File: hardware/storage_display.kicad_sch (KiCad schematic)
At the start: 0 parts

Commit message: Complete schematic, place and partially route the PCB
Schematic:
- Add Storage & Display sheet (microSD, FH12 OLED connector, TLV75801
  3.8 V VBAT regulator, charge-pump parts) and Radio sheet fixes
- Select remaining parts (PTS810, 1206L075THYR, SMF5.0A, MCP120 EN
  supervisor DNP, Elna DSK backup cap), add mounting holes and fiducials
- Pin changes for routability: PPS -> IO15, LoRa MOSI -> IO47,
  LoRa RESET -> IO48, LoRa DIO0 -> IO1
- Remove optional SPI clock filter parts (R309/C307, R310/C308)
- Remove company name from title blocks (personal project)

PCB (60 x 120 mm, 4 layers):
- Place all parts; GNSS zone with custom DRC rules (kicad_dru)
- Project ESP32-S3-WROOM-1 footprint with 0.4 mm thermal vias
- GND / +3V3 / +5V copper zones
- Route power path, GNSS, microSD and LoRa buses
- DRC clean except unrouted nets and expected silkscreen-at-edge items

Docs: selected-parts table, pin table and EMC deviation in PCB_DESIGN.md

Co-Authored-By: Claude Opus 5.5 <noreply@anthropic.com>
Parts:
- added C501: 100uF, Capacitor_SMD:C_1210_3225Metric, symbol Device:C
- added C502: 10uF, Capacitor_SMD:C_0805_2012Metric, symbol Device:C
- added C503: 100nF, Capacitor_SMD:C_0402_1005Metric, symbol Device:C
- added C504, C505, C506, C507, C510, C511: 1uF, Capacitor_SMD:C_0402_1005Metric, symbol Device:C
- added C508: 2.2uF, Capacitor_SMD:C_0603_1608Metric, symbol Device:C
- added C509: 4.7uF, Capacitor_SMD:C_0603_1608Metric, symbol Device:C
- added J501: DM3AT-SF-PEJM5, Connector_Card:microSD_HC_Hirose_DM3AT-SF-PEJM5, symbol Connector:Micro_SD_Card_Det2
- added J502: FH12-30S-0.5SH(55), Connector_FFC-FPC:Hirose_FH12-30S-0.5SH_1x30-1MP_P0.50mm_Horizontal, symbol Connector_Generic_MountingPin:Conn_01x30_MountingPin
- added R501, R502, R503, R504: 47k, Resistor_SMD:R_0402_1005Metric, symbol Device:R
- added R505, R510: 10k, Resistor_SMD:R_0402_1005Metric, symbol Device:R
- added R506, R507: 4.7k, Resistor_SMD:R_0402_1005Metric, symbol Device:R
- added R508: 390k, Resistor_SMD:R_0402_1005Metric, symbol Device:R
- added R509: 59k, Resistor_SMD:R_0402_1005Metric, symbol Device:R
- added TP501: VBAT, TestPoint:TestPoint_Pad_D1.0mm, symbol Connector:TestPoint
- added U501: TLV75801PDBV, Package_TO_SOT_SMD:SOT-23-5, symbol Regulator_Linear:TLV75801PDBV
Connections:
- new net: R509.2, R510.1, U501.4 (FB)
- new net +3V3: C501.1, C502.1, C503.1, C507.1, J501.4 (VDD), J502.11 (Pin_11), J502.9 (Pin_9), R501.1, R502.1, R503.1, R504.1, R505.1, R506.1, R507.1
- new net +5V: C510.1, U501.1 (IN), U501.3 (EN)
- new net GND: C501.2, C502.2, C503.2, C506.2, C507.2, C508.2, C509.2, C510.2, C511.2, J501.6 (VSS), J501.SH (SHIELD), J502.1 (Pin_1), J502.10 (Pin_10), J502.12 (Pin_12), J502.13 (Pin_13), J502.15 (Pin_15), J502.16 (Pin_16), J502.17 (Pin_17), J502.21 (Pin_21), J502.22 (Pin_22), J502.23 (Pin_23), J502.24 (Pin_24), J502.25 (Pin_25), J502.29 (Pin_29), J502.30 (Pin_30), J502.8 (Pin_8), J502.MP (MountPin), R508.2, R510.2, U501.2 (GND)
- new net OLED_C1N: C505.2, J502.5 (Pin_5)
- new net OLED_C1P: C505.1, J502.4 (Pin_4)
- new net OLED_C2N: C504.2, J502.2 (Pin_2)
- new net OLED_C2P: C504.1, J502.3 (Pin_3)
- new net OLED_IREF: J502.26 (Pin_26), R508.1
- new net OLED_RES: J502.14 (Pin_14), R505.2
- new net OLED_SCL: J502.18 (Pin_18), R507.2
- new net OLED_SDA: J502.19 (Pin_19), J502.20 (Pin_20), R506.2
- new net OLED_VBAT: C506.1, C511.1, J502.6 (Pin_6), R509.1, TP501.1, U501.5 (OUT)
- new net OLED_VCC: C508.1, J502.28 (Pin_28)
- new net OLED_VCOMH: C509.1, J502.27 (Pin_27)
- new net SD_CS: J501.2 (DAT3/CD), R502.2
- new net SD_DAT1: J501.8 (DAT1), R504.2
- new net SD_DAT2: J501.1 (DAT2), R501.2
- new net SD_MISO: J501.7 (DAT0), R503.2
- new net SD_MOSI: J501.3 (CMD)
- new net SD_SCK: J501.5 (CLK)
- no-connect marks 0 -> 3
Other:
- note added: "47k pull-ups on CS, DAT0, DAT1, DAT2. Card detect unused in v1."
- note added: "C504/C505 charge pump, C508 VCC, C509 VCOMH, R508 IREF"
- note added: "OLED: EastRising ER-OLED0.96-1.1W on Hirose FH12 (bottom contact). Values from panel datasheet sec. 1.6.2."
- note added: "Pin = panel FPC pin"
- note added: "VBAT 3.8 V: Vout = 0.55 V x (1 + 59k/10k) = 3.795 V (panel window 3.5-4.2 V). VCC/VCOMH caps rated 16 V or more."
- note added: "microSD (SPI mode, 3.3 V)"
- company: SSS-Defence -> (none)

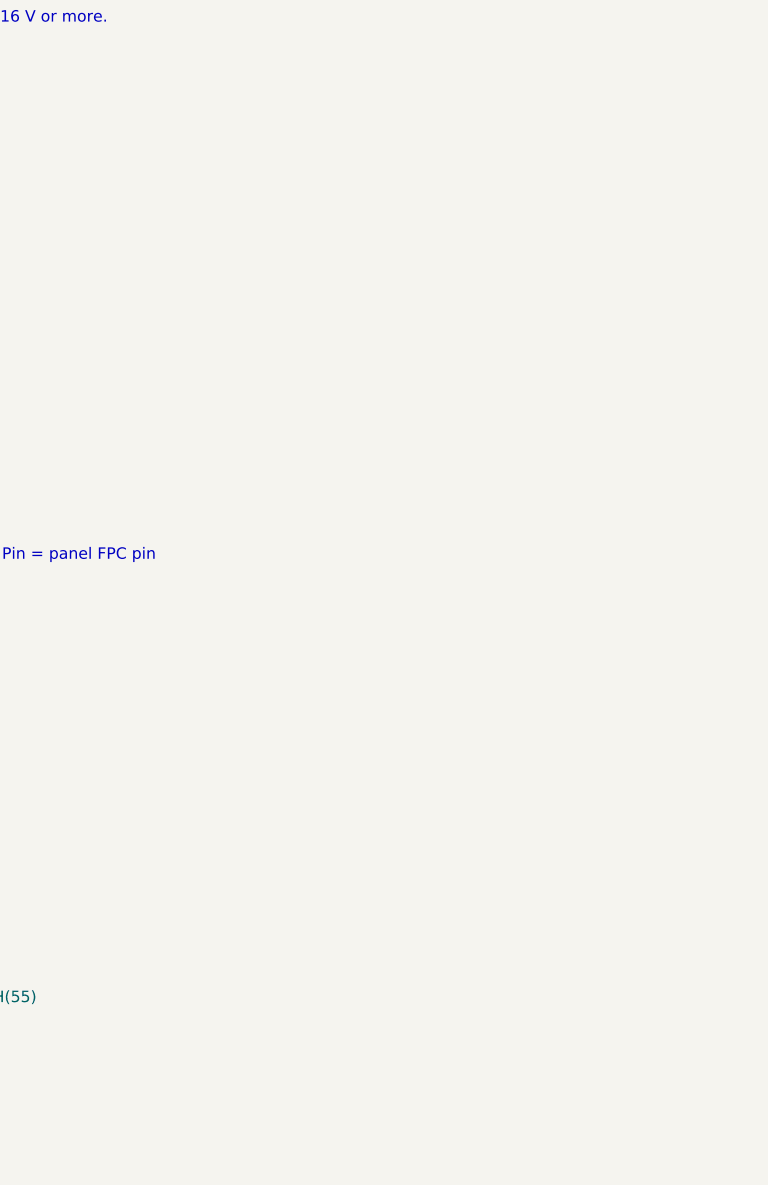
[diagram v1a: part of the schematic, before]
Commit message: Finish PCB routing, add BOM part numbers and fab export
Routing (DRC: 0 errors, 0 unconnected; ERC: 0)
- Complete the remaining nets on top of the GUI routing; GND stitching
  grid and edge fence; every GND pad reaches the L2 plane
- Re-lay the microSD bus under USB D+ so the USBLC6 and VBUS TVS get
  direct GND vias; lift LoRa NSS/MISO/MOSI to clear the TVS via
- Reroute D-, VBUS sense, CC2, BOOT, OLED SDA/SCL, LED and TXD0_R; remove
  vias in pads (R205, R505, R204, R507, U301 pin 7)
- Placement tweaks: C306 moved, C508/C509/R508 rotated 180, R302 moved
- PCB title block with rev v0.1

Parts and outputs
- MPN and Manufacturer fields on all placed parts (tools/add-mpn.py)
- tools/fab-export.py: ERC/DRC gate, zone refill, Gerbers, drill, BOM,
  pick-and-place and fab notes for Lion Circuits
- OLED panel DS501: schematic symbol and board-only 3D footprint
- Elna DSK footprint for C403 (not placed yet)
- kicad-routing skill under .claude/skills

Open before fab (see docs/PCB_DESIGN.md Open items): J502 pin order is
mirrored against the panel FPC; Lion stackup widths; C403 placement.

Co-Authored-By: Claude Opus 5.5 <noreply@anthropic.com>
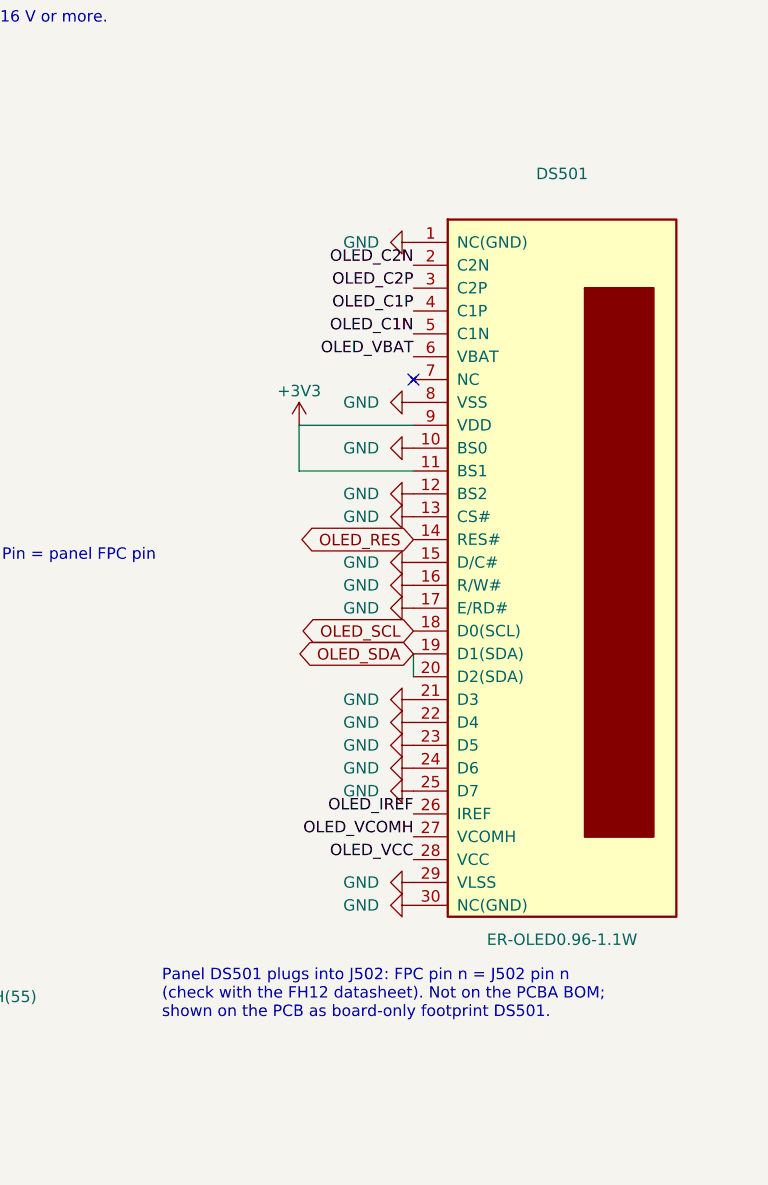
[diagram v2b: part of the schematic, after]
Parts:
- added DS501: ER-OLED0.96-1.1W, gps-lora:OLED_ER-OLED0.96-1.1W, symbol gps-lora:ER-OLED0.96-1.1W
- C501: MPN (none) -> GRM32ER61A107ME20L; Manufacturer (none) -> Murata
- C502: MPN (none) -> CL21A106KAYNNNE; Manufacturer (none) -> Samsung
- C503: MPN (none) -> CL05B104KO5NNNC; Manufacturer (none) -> Samsung
- C504, C505, C506, C507, C510, C511: MPN (none) -> CL05A105KA5NQNC; Manufacturer (none) -> Samsung
- C508: MPN (none) -> GRM188R61E225KA12D; Manufacturer (none) -> Murata
- C509: MPN (none) -> C1608X7R1C475K080AC; Manufacturer (none) -> TDK
- J501: MPN (none) -> DM3AT-SF-PEJM5; Manufacturer (none) -> Hirose
- J502: MPN (none) -> FH12-30S-0.5SH(55); Manufacturer (none) -> Hirose
- R501, R502, R503, R504: MPN (none) -> RC0402FR-0747KL; Manufacturer (none) -> Yageo
- R505, R510: MPN (none) -> RC0402FR-0710KL; Manufacturer (none) -> Yageo
- R506, R507: MPN (none) -> RC0402FR-074K7L; Manufacturer (none) -> Yageo
- R508: MPN (none) -> RC0402FR-07390KL; Manufacturer (none) -> Yageo
- R509: MPN (none) -> RC0402FR-0759KL; Manufacturer (none) -> Yageo
- U501: MPN (none) -> TLV75801PDBVR; Manufacturer (none) -> Texas Instruments
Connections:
- net +3V3: now also DS501.11 (BS1), DS501.9 (VDD)
- net GND: now also DS501.1 (NC(GND)), DS501.10 (BS0), DS501.12 (BS2), DS501.13 (CS#), DS501.15 (D/C#), DS501.16 (R/W#), DS501.17 (E/RD#), DS501.21 (D3), DS501.22 (D4), DS501.23 (D5), DS501.24 (D6), DS501.25 (D7), DS501.29 (VLSS), DS501.30 (NC(GND)), DS501.8 (VSS)
- net OLED_C1N: now also DS501.5 (C1N)
- net OLED_C1P: now also DS501.4 (C1P)
- net OLED_C2N: now also DS501.2 (C2N)
- net OLED_C2P: now also DS501.3 (C2P)
- net OLED_IREF: now also DS501.26 (IREF)
- net OLED_RES: now also DS501.14 (RES#)
- net OLED_SCL: now also DS501.18 (D0(SCL))
- net OLED_SDA: now also DS501.19 (D1(SDA)), DS501.20 (D2(SDA))
- net OLED_VBAT: now also DS501.6 (VBAT)
- net OLED_VCC: now also DS501.28 (VCC)
- net OLED_VCOMH: now also DS501.27 (VCOMH)
- no-connect marks 3 -> 4
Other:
- note added: "Panel DS501 plugs into J502: FPC pin n = J502 pin n (check with the FH12 datasheet). Not on the PCBA BOM; shown on the PCB as board-only footprint DS501."

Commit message: Rename project to Theoros and add V1.0 silkscreen artwork
Theoros (Greek θεωρός): an official observer and envoy, sent to watch
and report back.

Rename gps-lora to theoros everywhere: KiCad project, symbol and
footprint libraries, firmware library (theoros-core), umbrella header,
PC tool (tools/theoros.py), NVS namespaces, mDNS hostname, docs and
title blocks. The HKDF salt is now "theoros" (7 bytes), so every derived
key changes; the SECURITY.md test vectors are recomputed and host tests
pass. Boards provisioned with the old salt need re-provisioning.

Board revision is now V1.0. Silkscreen additions:
- Top: "THEOROS ${REVISION}" and "ΘΕΩΡΟΣ", an antenna warning next to
  J401, and a hidden line under the OLED panel.
- Bottom: an owl made as a solder-mask opening over the GND pour (gold
  with ENIG; vias inside stay tented) and the motto "ΟΡΩ ΚΑΙ ΑΓΓΕΛΛΩ /
  I SEE AND I REPORT".
Fab notes now state silkscreen on both sides and the intentional mask
opening. DRC is unchanged from before (4 silk-edge warnings).

Co-Authored-By: Claude Opus 5.5 <noreply@anthropic.com>
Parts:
- DS501: footprint gps-lora:OLED_ER-OLED0.96-1.1W -> theoros:OLED_ER-OLED0.96-1.1W; symbol gps-lora:ER-OLED0.96-1.1W -> theoros:ER-OLED0.96-1.1W

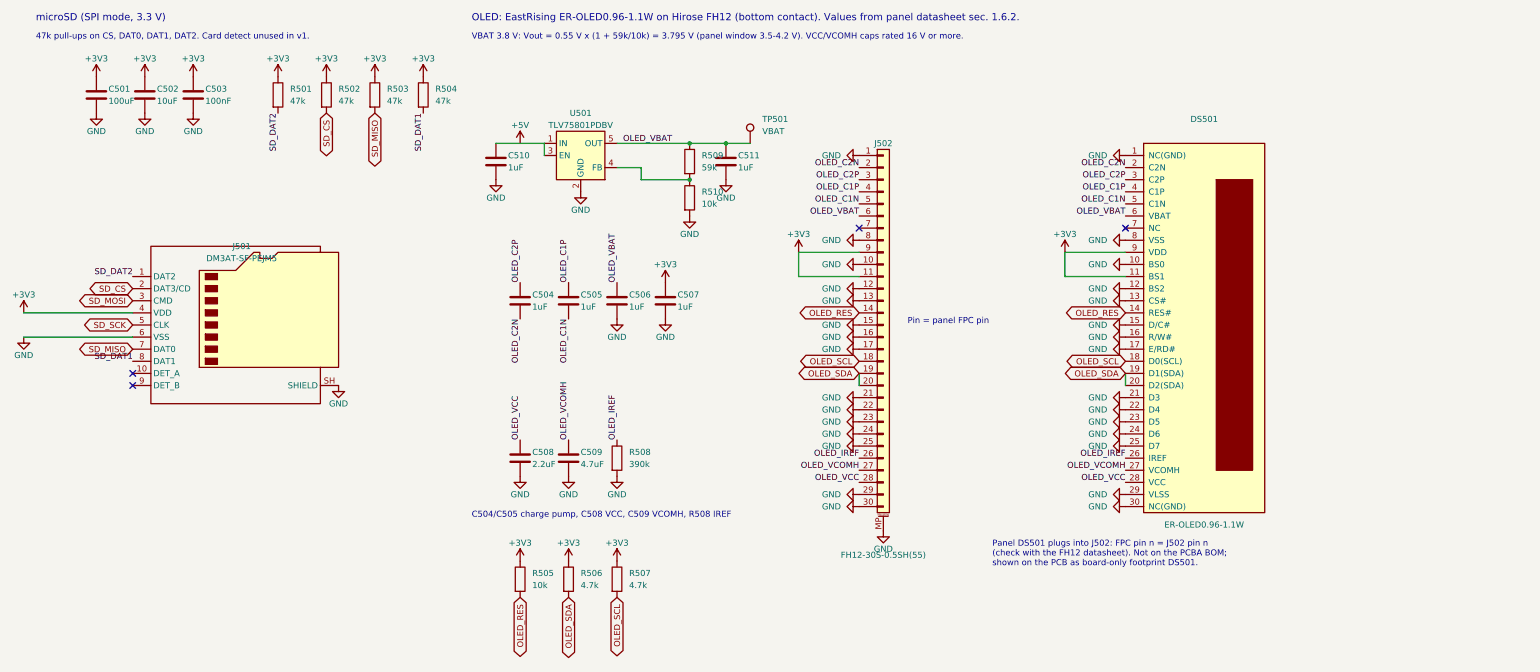
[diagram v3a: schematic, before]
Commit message: Fix J502 pin mapping, place C403 backup, check stackup impedance
J502: the panel FPC lands mirrored on the 180-degree FH12 (panel pin n on
J502 pin 31-n, per the ER-OLED0.96-1.1W drawing 1.4.1). The J502 symbol is
now mirrored in the schematic and the OLED support row is re-placed in the
new pin order and hand-routed. C305 (DNP) turns horizontal and R302 moves
0.4 mm east to make room.

C403: Seiko CPH3225A 11 mF chip EDLC on V_BCKP (~10 min hot-start
hold-up), with a new footprint from the Seiko drawing (pad 1 = +). D401
and R401, which charge it from 3V3, are now fitted. The unused Elna
footprint is removed.

Stackup: Lion's standard 4-layer 1.6 mm build (2116, 0.12 mm to L2) gives
47-49 ohm on LORA_ANT and 89-100 ohm on the USB pair with the existing
0.2 mm traces, so no impedance-controlled order is needed.

DRC: same 4 silk-edge warnings as before, 0 unconnected, schematic parity
clean. ERC clean.

Co-Authored-By: Claude Opus 5.5 <noreply@anthropic.com>
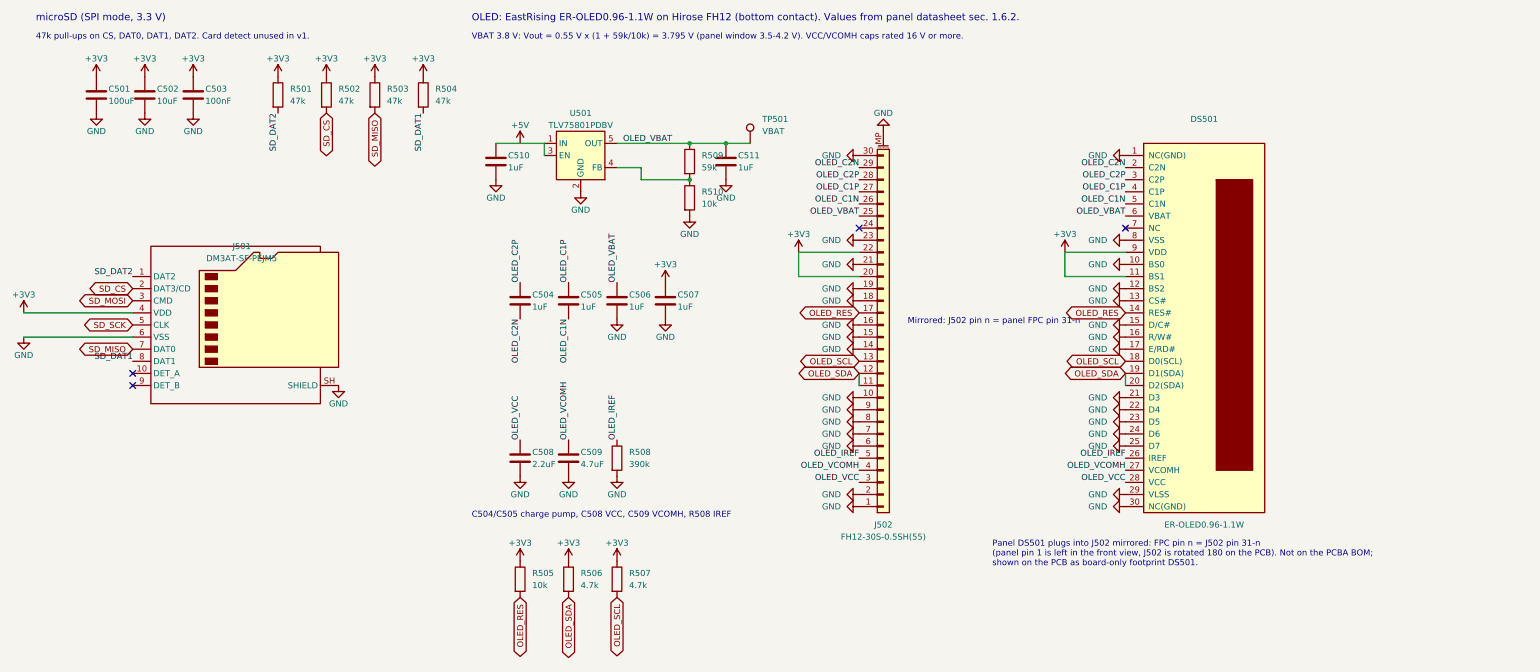
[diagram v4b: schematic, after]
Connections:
- net +3V3: now also J502.20 (Pin_20), J502.22 (Pin_22); no longer J502.11 (Pin_11), J502.9 (Pin_9)
- net GND: now also J502.14 (Pin_14), J502.18 (Pin_18), J502.19 (Pin_19), J502.2 (Pin_2), J502.6 (Pin_6), J502.7 (Pin_7), J502.9 (Pin_9); no longer J502.12 (Pin_12), J502.13 (Pin_13), J502.17 (Pin_17), J502.22 (Pin_22), J502.24 (Pin_24), J502.25 (Pin_25), J502.29 (Pin_29)
- net OLED_C1N: now also J502.26 (Pin_26); no longer J502.5 (Pin_5)
- net OLED_C1P: now also J502.27 (Pin_27); no longer J502.4 (Pin_4)
- net OLED_C2N: now also J502.29 (Pin_29); no longer J502.2 (Pin_2)
- net OLED_C2P: now also J502.28 (Pin_28); no longer J502.3 (Pin_3)
- net OLED_IREF: now also J502.5 (Pin_5); no longer J502.26 (Pin_26)
- net OLED_RES: now also J502.17 (Pin_17); no longer J502.14 (Pin_14)
- net OLED_SCL: now also J502.13 (Pin_13); no longer J502.18 (Pin_18)
- net OLED_SDA: now also J502.11 (Pin_11), J502.12 (Pin_12); no longer J502.19 (Pin_19), J502.20 (Pin_20)
- net OLED_VBAT: now also J502.25 (Pin_25); no longer J502.6 (Pin_6)
- net OLED_VCC: now also J502.3 (Pin_3); no longer J502.28 (Pin_28)
- net OLED_VCOMH: now also J502.4 (Pin_4); no longer J502.27 (Pin_27)
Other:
- note added: "Mirrored: J502 pin n = panel FPC pin 31-n"
- note added: "Panel DS501 plugs into J502 mirrored: FPC pin n = J502 pin 31-n (panel pin 1 is left in the front view, J502 is rotated 180 on the PCB). Not on the PCBA BOM; shown on the PCB as board-only footprint DS501."
- note removed: "Panel DS501 plugs into J502: FPC pin n = J502 pin n (check with the FH12 datasheet). Not on the PCBA BOM; shown on the PCB as board-only footprint DS501."
- note removed: "Pin = panel FPC pin"
- moved on the sheet: J502
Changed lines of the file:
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@@
 		(comment 2 "https://github.com/Majorwhiskey/theoros")
 	)
-	(text "Pin = panel FPC pin"
+	(text "Mirrored: J502 pin n = panel FPC pin 31-n"
 		(exclude_from_sim no)
 		(at 208.28 101.6 0)
@@
 	(symbol
 		(lib_id "Connector_Generic_MountingPin:Conn_01x30_MountingPin")
-		(at 203.2 101.6 0)
+		(at 203.2 104.14 0)
+		(mirror x)
 		(unit 1)
 		(body_style 1)
@@
 		(dnp no)
 		(property "Reference" "J502"
-			(at 203.2 63.5 0)
+			(at 203.2 143.51 0)
 			(show_name no)
 			(do_not_autoplace no)
@@
 		)
 		(property "Value" "FH12-30S-0.5SH(55)"
-			(at 203.2 149.86 0)
+			(at 203.2 146.05 0)
 			(show_name no)
 			(do_not_autoplace no)
@@
 	(symbol
 		(lib_id "power:GND")
-		(at 203.2 144.78 0)
+		(at 203.2 60.96 180)
 		(unit 1)
 		(body_style 1)
@@
 		(dnp no)
 		(property "Reference" "#PWR544"
-			(at 203.2 144.78 0)
+			(at 203.2 60.96 0)
 			(hide yes)
 			(show_name no)
@@
 		)
 		(property "Value" "GND"
-			(at 203.2 148.59 0)
+			(at 203.2 57.15 0)
 			(show_name no)
 			(do_not_autoplace no)
@@
 		)
 		(property "Footprint" ""
-			(at 203.2 144.78 0)
+			(at 203.2 60.96 0)
 			(hide yes)
 			(show_name no)
@@
 		)
 		(property "Datasheet" ""
-			(at 203.2 144.78 0)
+			(at 203.2 60.96 0)
 			(hide yes)
 			(show_name no)
@@
 		)
 		(property "Description" "Power symbol creates a global label with name \"GND\" , ground"
-			(at 203.2 144.78 0)
+			(at 203.2 60.96 0)
 			(hide yes)
 			(show_name no)
@@
 		)
 	)
-	(text "Panel DS501 plugs into J502: FPC pin n = J502 pin n\n(check with the FH12 datasheet). Not on the PCBA BOM;\nshown on the PCB as board-only footprint DS501."
+	(text "Panel DS501 plugs into J502 mirrored: FPC pin n = J502 pin 31-n\n(panel pin 1 is left in the front view, J502 is rotated 180 on the PCB). Not on the PCBA BOM;\nshown on the PCB as board-only footprint DS501."
 		(exclude_from_sim no)
 		(at 226.06 152.4 0)
